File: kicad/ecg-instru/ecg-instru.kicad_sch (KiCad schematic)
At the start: 24 parts, among them J2 Screw_Terminal_01x02, J3 Screw_Terminal_01x03, J4 Conn_01x02_Socket, J5 Conn_01x02_Socket, J6 Conn_01x08_Socket, U1 LM324, U2 INA128, U3 YAAJ_BluePill

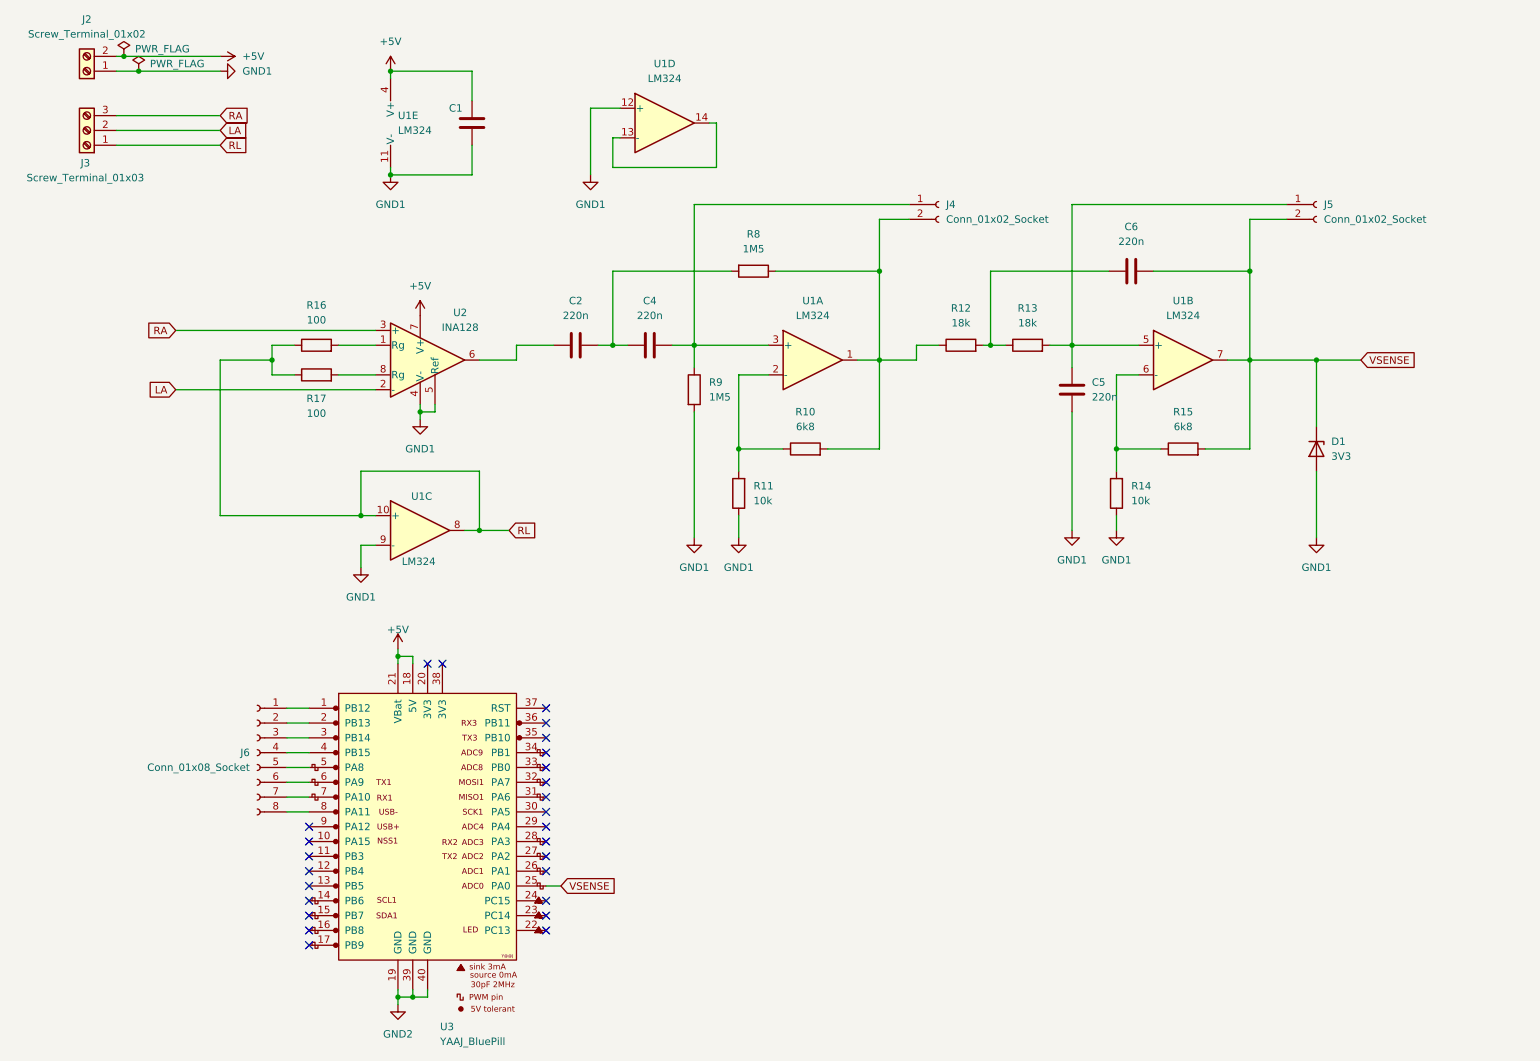
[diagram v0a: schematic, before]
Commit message: New schematic with correct components
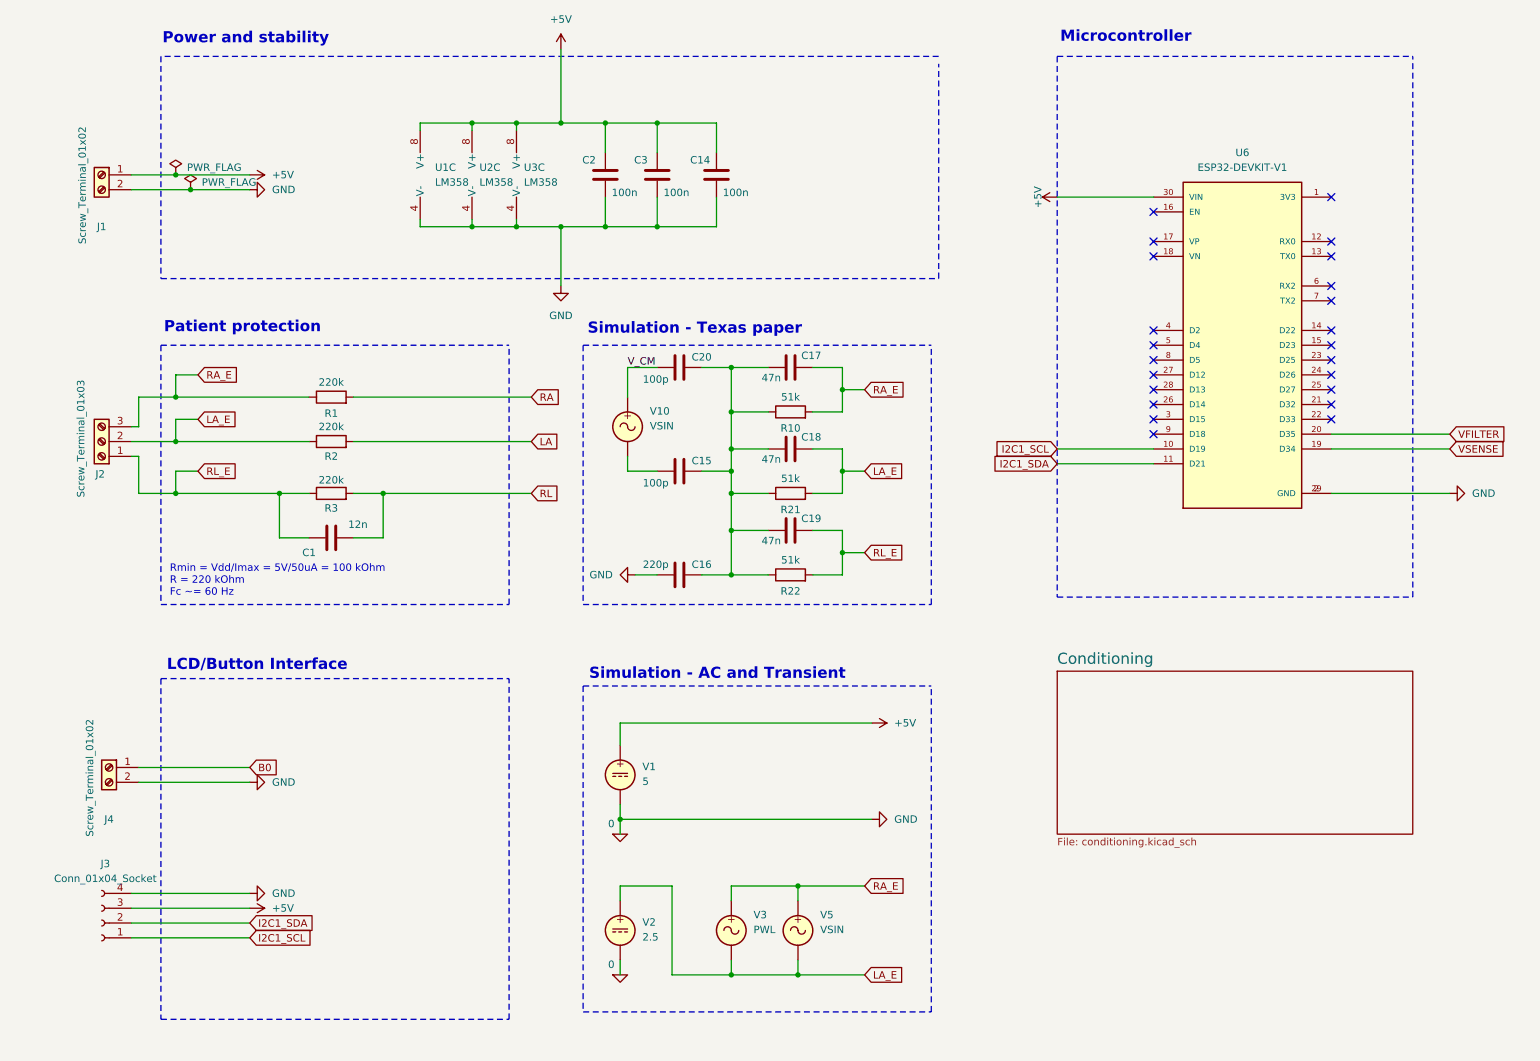
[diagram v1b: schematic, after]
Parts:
- removed C2, C4, C5, C6: 220n, Capacitor_THT:C_Rect_L7.0mm_W2.5mm_P5.00mm, symbol Device:C
- removed D1: 3V3, symbol Device:D_Zener
- removed J4, J5: Conn_01x02_Socket, Connector_PinHeader_2.54mm:PinHeader_1x02_P2.54mm_Vertical, symbol Connector:Conn_01x02_Socket
- removed J6: Conn_01x08_Socket, symbol Connector:Conn_01x08_Socket
- removed R11, R14: 10k, Resistor_THT:R_Axial_DIN0309_L9.0mm_D3.2mm_P15.24mm_Horizontal, symbol Device:R
- removed R12, R13: 18k, Resistor_THT:R_Axial_DIN0309_L9.0mm_D3.2mm_P15.24mm_Horizontal, symbol Device:R
- removed R15: 6k8, Resistor_THT:R_Axial_DIN0309_L9.0mm_D3.2mm_P15.24mm_Horizontal, symbol Device:R
- removed R16, R17: 100, Resistor_THT:R_Axial_DIN0309_L9.0mm_D3.2mm_P15.24mm_Horizontal, symbol Device:R
- removed R8, R9: 1M5, Resistor_THT:R_Axial_DIN0309_L9.0mm_D3.2mm_P15.24mm_Horizontal, symbol Device:R
- removed U1: LM324, symbol Amplifier_Operational:LM324
- removed U2: INA128, symbol Amplifier_Instrumentation:INA128
- removed U3: YAAJ_BluePill, STM32:YAAJ_BluePill_1, symbol YAAJ_BluePill:YAAJ_BluePill
- added C1: 12n, Capacitor_THT:C_Rect_L7.0mm_W2.5mm_P5.00mm, symbol Device:C
- added C14, C3: 100n, Capacitor_THT:C_Rect_L7.0mm_W2.5mm_P5.00mm, symbol Device:C
- added C15, C20: 100p, Capacitor_THT:C_Rect_L7.0mm_W2.5mm_P5.00mm, symbol Device:C
- added C16: 220p, Capacitor_THT:C_Rect_L7.0mm_W2.5mm_P5.00mm, symbol Device:C
- added C17, C18, C19: 47n, Capacitor_THT:C_Rect_L7.0mm_W2.5mm_P5.00mm, symbol Device:C
- added J3: Conn_01x04_Socket, Connector_PinHeader_2.54mm:PinHeader_1x04_P2.54mm_Vertical, symbol Connector:Conn_01x04_Socket
- added J4: Screw_Terminal_01x02, TerminalBlock:TerminalBlock_MaiXu_MX126-5.0-02P_1x02_P5.00mm, symbol Connector:Screw_Terminal_01x02
- added R1, R2, R3: 220k, Resistor_THT:R_Axial_DIN0309_L9.0mm_D3.2mm_P15.24mm_Horizontal, symbol Device:R
- added R21, R22: 51k, Resistor_THT:R_Axial_DIN0309_L9.0mm_D3.2mm_P15.24mm_Horizontal, symbol Device:R
- added U1, U2, U3: LM358, Package_DIP:DIP-8_W7.62mm_LongPads, symbol Amplifier_Operational:LM358
- added U6: ESP32-DEVKIT-V1, ESP32-DEVKIT-V1:MODULE_ESP32_DEVKIT_V1, symbol ESP32-DEVKIT-V1:ESP32-DEVKIT-V1
- added V1: 5, symbol Simulation_SPICE:VDC
- added V10, V5: VSIN, symbol Simulation_SPICE:VSIN
- added V2: 2.5, symbol Simulation_SPICE:VDC
- added V3: PWL, symbol Simulation_SPICE:VSIN
- R10: value 6k8 -> 51k
- renumbered C1 to C2, J2 to J1, J3 to J2
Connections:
- net +5V: now also J1.1 (Pin_1), C14.2, C3.2, J3.3 (Pin_3), U1.8 (V+), U2.8 (V+), U3.8 (V+), U6.30 (VIN), V1.1; no longer J1.2 (Pin_2)
- net LA: now also R2.2; no longer J2.2 (Pin_2)
- net RA: now also R1.2; no longer J2.3 (Pin_3)
- net RL: now also C1.1, R3.2; no longer J2.1 (Pin_1)
- net VSENSE: now also U6.19 (D34)
- net RA_E: now reaches R10.2
- net RA_E: now also J2.3 (Pin_3), C17.2, R1.1, V3.1, V5.1
- net at R10.1: now also C15.2, C16.2, C17.1, C18.1, C19.1, C20.2, R21.1, R22.1
- net GND1 renamed 0
- net 0: now also J1.2 (Pin_2), C14.1, C16.1, C3.1, J3.4 (Pin_4), J4.2 (Pin_2), U1.4 (V-), U2.4 (V-), U3.4 (V-), U6.2 (GND), U6.29 (GND), V1.2, V2.2; no longer J1.1 (Pin_1)
- new net: C15.1, V10.2
- new net B0: J4.1 (Pin_1)
- new net I2C1_SCL: J3.1 (Pin_1), U6.10 (D19)
- new net I2C1_SDA: J3.2 (Pin_2), U6.11 (D21)
- new net LA_E: C18.2, J2.2 (Pin_2), R2.1, R21.2, V2.1, V3.2, V5.2
- new net RL_E: C1.2, C19.2, J2.1 (Pin_1), R22.2, R3.1
- new net VFILTER: U6.20 (D35)
- new net V_CM: C20.1, V10.1
- no-connect marks 26 -> 23
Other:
- added sheet Conditioning (conditioning.kicad_sch)
- note added: "LCD/Button Interface"
- note added: "Microcontroller"
- note added: "Patient protection"
- note added: "Power and stability"
- note added: "Rmin = Vdd/Imax = 5V/50uA = 100 kOhm R = 220 kOhm Fc ~= 60 Hz"
- note added: "Simulation - AC and Transient"
- note added: "Simulation - Texas paper"
- moved on the sheet: C2, J1, J2

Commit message: Board layout + Schematic + ESP32 initial src
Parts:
- removed J3: Conn_01x04_Socket, Connector_PinHeader_2.54mm:PinHeader_1x04_P2.54mm_Vertical, symbol Connector:Conn_01x04_Socket
- removed J4: Screw_Terminal_01x02, TerminalBlock:TerminalBlock_MaiXu_MX126-5.0-02P_1x02_P5.00mm, symbol Connector:Screw_Terminal_01x02
- added J3: Conn_01x02_Socket, Connector_PinHeader_2.54mm:PinHeader_1x02_P2.54mm_Vertical, symbol Connector:Conn_01x02_Socket
- added J6: Conn_01x06_Socket, Connector_PinHeader_2.54mm:PinHeader_1x06_P2.54mm_Vertical, symbol Connector:Conn_01x06_Socket
- R1, R10, R2, R21, R22, R3: footprint Resistor_THT:R_Axial_DIN0309_L9.0mm_D3.2mm_P15.24mm_Horizontal -> Resistor_THT:R_Axial_DIN0309_L9.0mm_D3.2mm_P12.70mm_Horizontal
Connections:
- net +5V: now also J6.5 (Pin_5)
- net 0: now also J6.6 (Pin_6)
- net B0: now also U6.14 (D22), J6.2 (Pin_2)
- net I2C1_SCL: now also U6.13 (TX0), J6.3 (Pin_3); no longer U6.10 (D19)
- net I2C1_SDA: now also U6.12 (RX0), J6.4 (Pin_4); no longer U6.11 (D21)
- net LA: now also R1.2; no longer R2.2
- net LA_E: now also J2.1 (Pin_1), R1.1; no longer J2.2 (Pin_2), R2.1
- net RA: now also R2.2; no longer R1.2
- net RA_E: now also J2.2 (Pin_2), R2.1; no longer J2.3 (Pin_3), R1.1
- net RL_E: now also J2.3 (Pin_3); no longer J2.1 (Pin_1)
- net VSENSE: now also J3.2 (Pin_2)
- net B1: now reaches U6.15 (D23)
- net B1: now also J6.1 (Pin_1)
- net VFILTER renamed VADC
- net VADC: now also J3.1 (Pin_1)
- no-connect marks 23 -> 20
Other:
- note added: "LCD/Button Interface + Outputs"
- note removed: "LCD/Button Interface"
- moved on the sheet: J2
